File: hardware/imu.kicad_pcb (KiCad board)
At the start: 4 copper layers, 40 x 40 mm, 108 parts, among them J1 USB-MINI-B-SMD, J2 DRILL, J3 DRILL, J4 DRILL, J5 DRILL, J6 STACK-UP-LOW, J7 STACK-DOWN, J8 STACK-UP-LOW, J9 STACK-DOWN, P1 CON-SENSOR, P2 CON-SENSOR, SW1 Reset, SW2 Erase, U1 AT91SAM3SXB, U2 82400152, U3 BNO055, U4 LD1117, X1 16Mhz, X2 32.768kHz

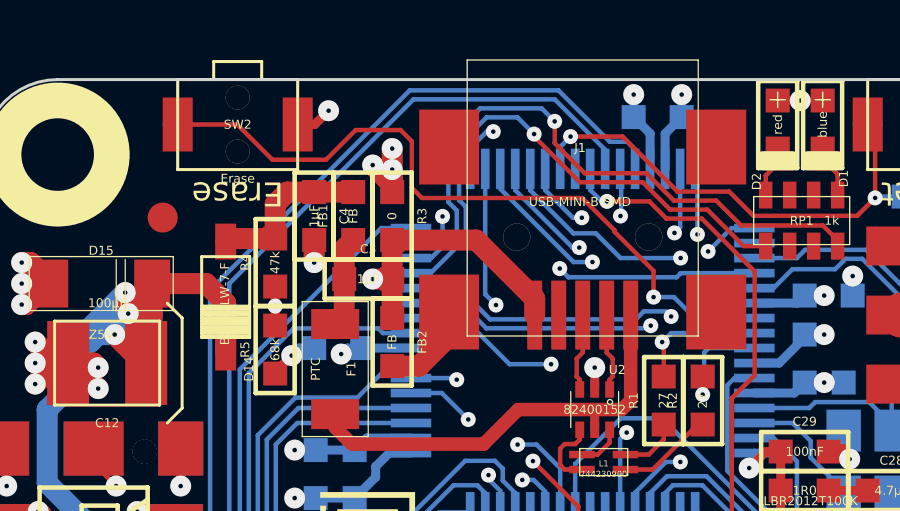
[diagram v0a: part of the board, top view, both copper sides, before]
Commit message: route signals with more distance to border
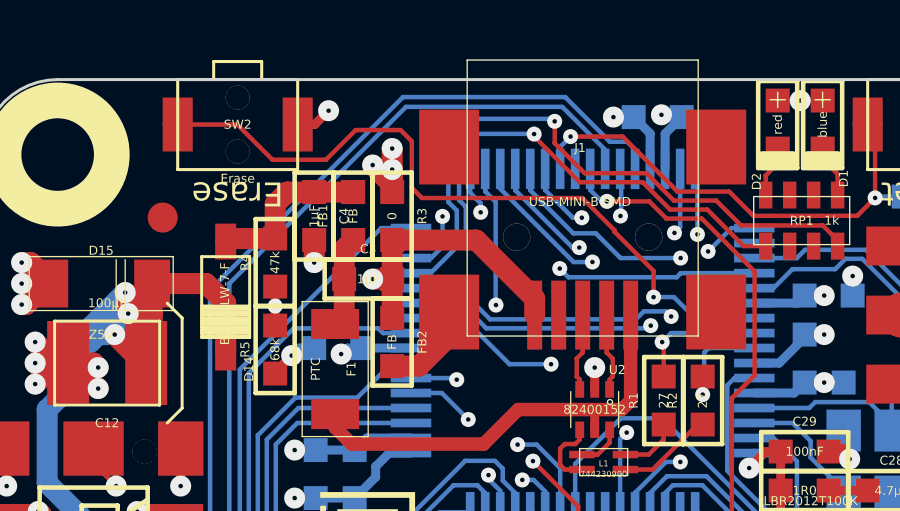
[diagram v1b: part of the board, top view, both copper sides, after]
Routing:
- net STACK-I2C-SDA/JTAG-TDI: track 27.9 -> 27.3 mm

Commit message: change footprint of bno055 crystal
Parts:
- X2: footprint CRYSTAL_3225 -> kicad-libraries:AB26TRQ
- moved C5 3.52 mm to (144.2, 107.5), turned to 180 degrees
- moved C6 2.91 mm to (144.2, 103.9)
- moved X2 1.14 mm to (141.6, 105.7), turned to 270 degrees
- moved R6 0.81 mm to (148.4, 107.5)
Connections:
- C5 pad 1: N-00000128 -> Net-(C5-Pad1)
- C6 pad 1: N-00000133 -> Net-(C6-Pad1)
- U3 pad 26: N-00000133 -> Net-(C6-Pad1)
- U3 pad 27: N-00000128 -> Net-(C5-Pad1)
- X2 pad 1: N-00000128 -> Net-(C6-Pad1)
- X2 pad 2: N-00000133 -> Net-(C5-Pad1)
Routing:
- net N-00000128: track 8.90 -> 0.00 mm, vias 1 -> 0
- net N-00000133: track 6.89 -> 0.00 mm, vias 1 -> 0
- net GND: track 407.8 -> 412.2 mm, vias 78 -> 80
- net Net-(C6-Pad1): track 0.00 -> 4.33 mm, vias 0 -> 1
- net Net-(C5-Pad1): track 0.00 -> 4.08 mm, vias 0 -> 1
- net BNO-BOOT: track 25.6 -> 24.8 mm
- added copper zone on B.Cu, net GND

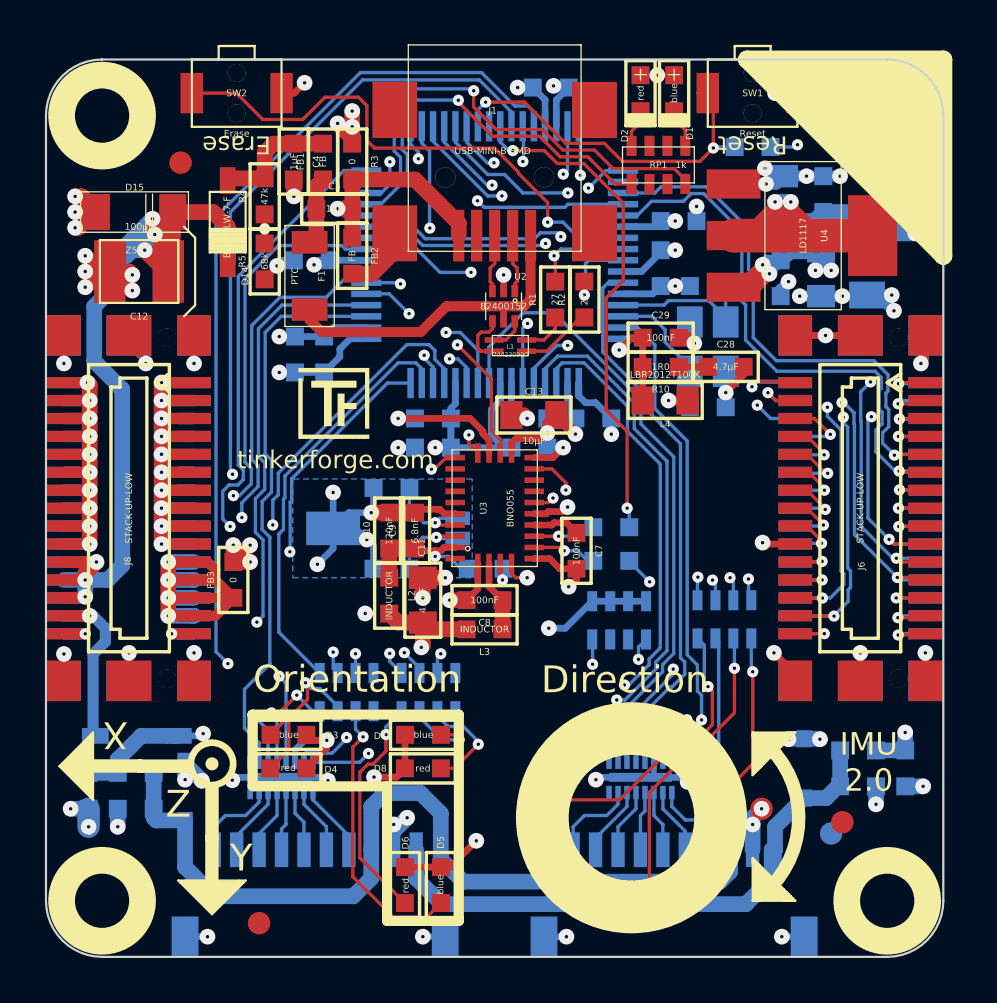
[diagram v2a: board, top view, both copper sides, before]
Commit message: fix tvs diode orientation, fix component texts
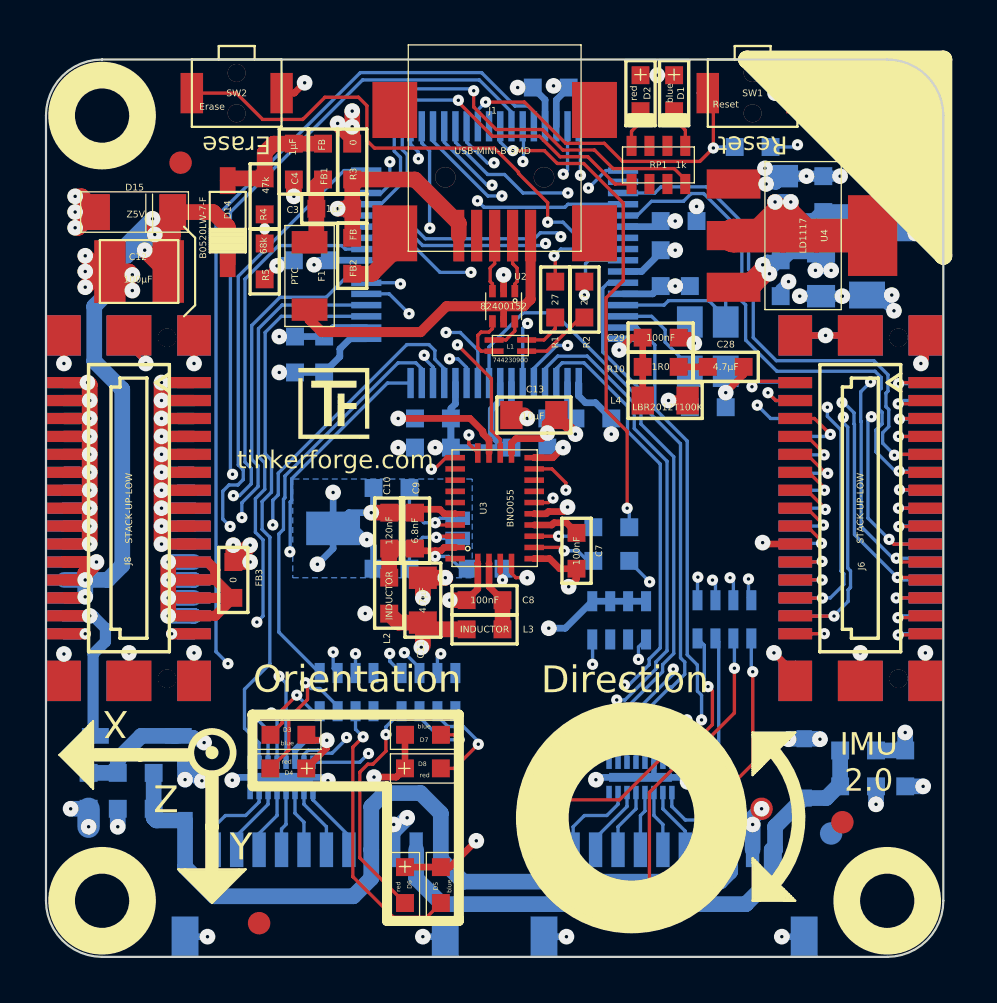
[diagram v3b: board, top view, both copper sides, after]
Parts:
- C1, C2: value 9pF -> DNP
- D10, D11, D12, D4, D6, D8, D9: footprint 0603 -> kicad-libraries:D0603
- D3, D5, D7: footprint 0603 -> kicad-libraries:0603
- turned D401 to 270 degrees
- turned D402 to 270 degrees
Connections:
- D401 pad 1: Net-(C403-Pad1) -> GND
- D401 pad 2: GND -> Net-(C403-Pad1)
- D402 pad 1: Net-(C404-Pad1) -> GND
- D402 pad 2: GND -> Net-(C404-Pad1)

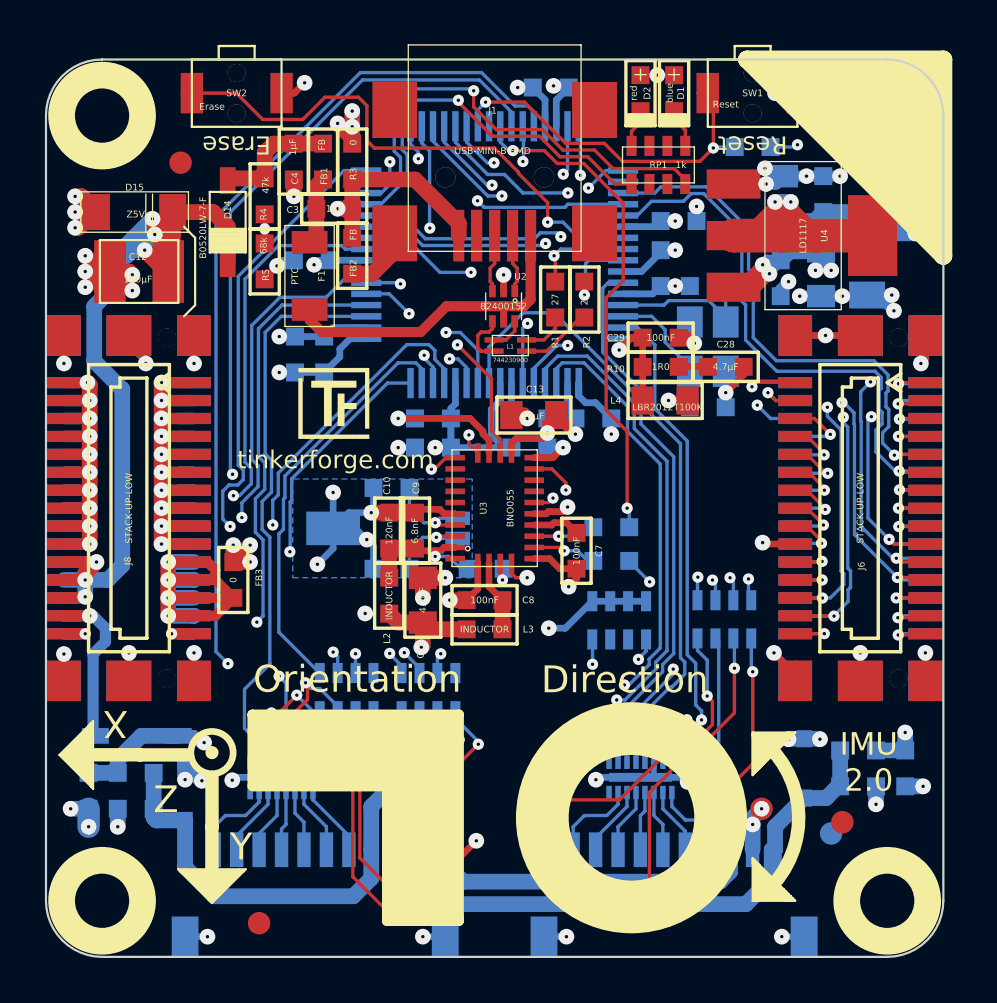
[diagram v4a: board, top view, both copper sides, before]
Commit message: fix diode symbols
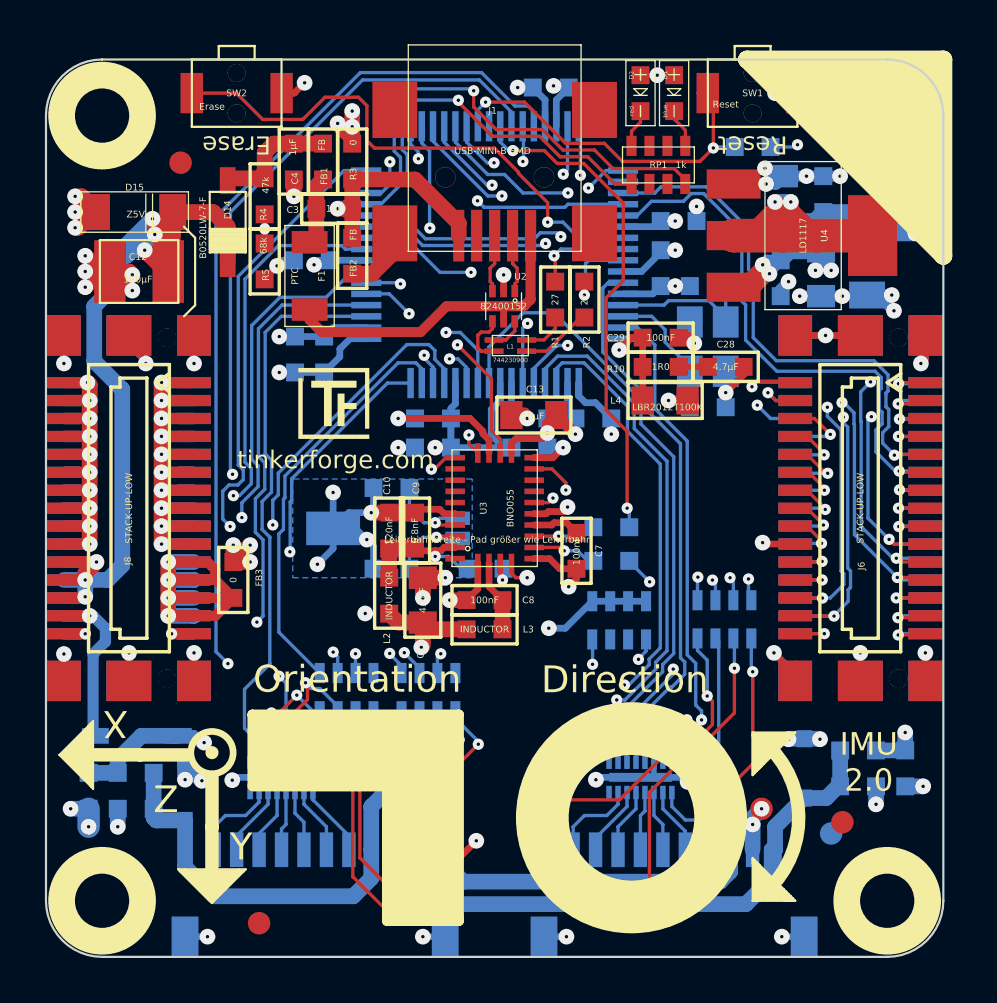
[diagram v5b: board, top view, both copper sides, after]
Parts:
- D1, D2: footprint D0603 -> kicad-libraries:D0603
- D3, D5, D7: footprint kicad-libraries:0603 -> kicad-libraries:D0603
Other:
- board text added: "Leiterbahnbreite - Pad größer wie Leiterbahn"

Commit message: Add some 3d components
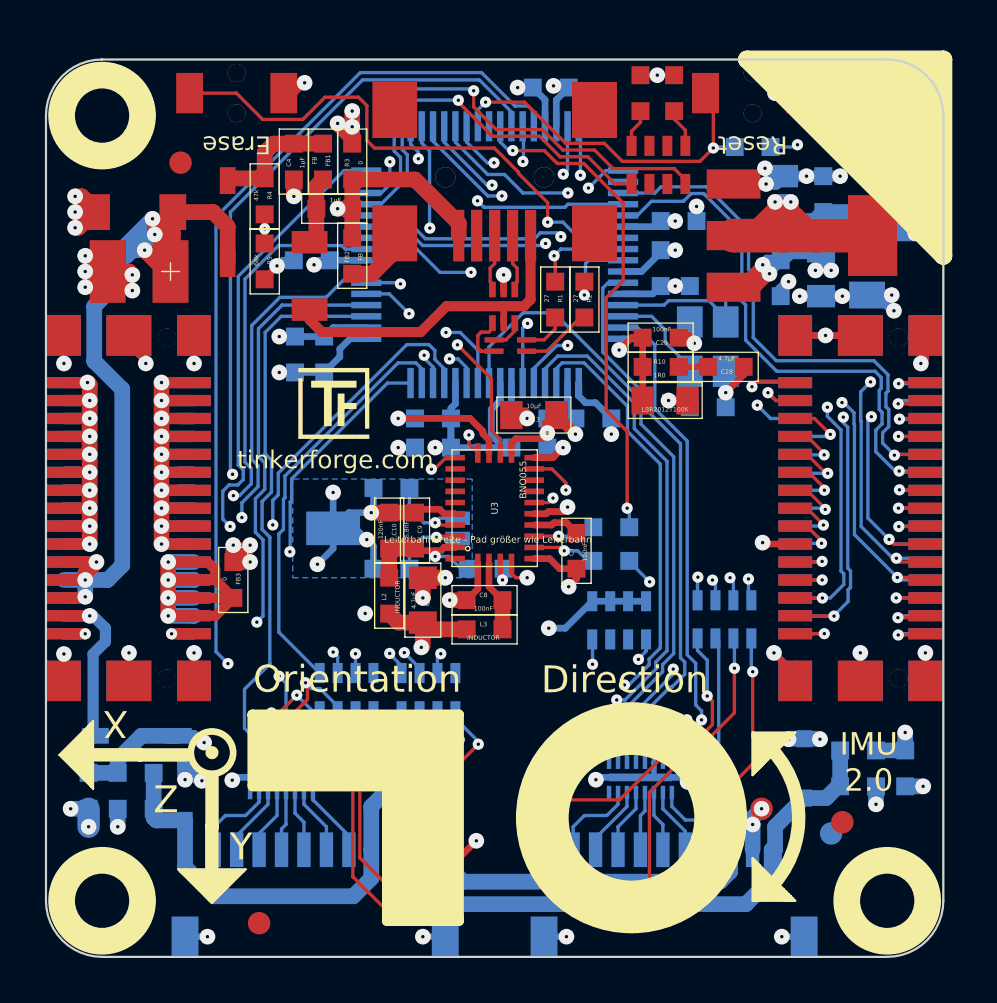
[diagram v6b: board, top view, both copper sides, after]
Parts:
- C1, C10, C14, C15, C17, C18, C19, C2, C20, C21, C22, C23, C24, C26, C27, C28, C29, C3, C30, C4, C401, C402, C403, C404, C5, C6, C7, C8, C9, FB1, FB2, FB3, FB4, FB401, FB402, L2, L3, R1, R10, R2, R3, R4, R5, R6, R7, R8, R9: footprint 0603 -> kicad-libraries:0603
- C11, C13, C16, C25, L4: footprint 0805 -> kicad-libraries:0805
- C12: footprint 3528-21 -> kicad-libraries:3528-21
- D13, D14: footprint SOD-123 -> kicad-libraries:SOD-123
- D15, D16: footprint MiniMelf -> kicad-libraries:MiniMelf
- D401, D402: footprint SOD-323 -> kicad-libraries:SOD-323
- F1: footprint 1206 -> kicad-libraries:1206
- FILTER401, FILTER402: footprint DFN16-33x135 -> kicad-libraries:DFN16-33x135
- J1: footprint USB-MINI-B-SMD -> kicad-libraries:USB-MINI-B-SMD
- J2, J3, J4, J5: footprint DRILL_NP -> kicad-libraries:DRILL_NP
- J6, J8: footprint BTB08-ACS-TOP -> kicad-libraries:BTB08-ACS-TOP
- J7, J9: footprint BTB08-ACS-BTM -> kicad-libraries:BTB08-ACS-BTM
- L1: footprint WE-CNSW-0603 -> kicad-libraries:WE-CNSW-0603
- P1, P2: footprint CON-SENSOR -> kicad-libraries:CON-SENSOR
- RP1, RP2, RP3, RP4, RP5: footprint 0603X4 -> kicad-libraries:0603X4
- SW1, SW2: footprint TACT-SWITCH -> kicad-libraries:TACT-SWITCH
- U1: footprint LQFP64 -> kicad-libraries:LQFP64
- U2: footprint SOT563-SPEC -> kicad-libraries:SOT563-SPEC
- U3: footprint LGA28_5832 -> kicad-libraries:LGA28_5832
- U4: footprint SOT-223 -> kicad-libraries:SOT-223
- X1: footprint CRYSTAL_3225 -> kicad-libraries:CRYSTAL_3225

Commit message: Add all 3d information
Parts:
- C1, C10, C14, C15, C17, C18, C19, C2, C20, C21, C22, C23, C24, C26, C27, C28, C29, C30, C4, C401, C402, C403, C404, C5, C6, C7, C8, C9, FB1, FB2, FB3, FB4, L2, L3: footprint kicad-libraries:0603 -> kicad-libraries:C0603
- C11, C13, C16, C25, L4: footprint kicad-libraries:0805 -> kicad-libraries:C0805
- F1: footprint kicad-libraries:1206 -> kicad-libraries:C1206
- FB401, FB402: footprint kicad-libraries:0603 -> C0603
- FILTER401, FILTER402: footprint kicad-libraries:DFN16-33x135 -> DFN16-33x135
- R1, R10, R2, R3, R4, R5, R6, R7, R8, R9: footprint kicad-libraries:0603 -> kicad-libraries:R0603
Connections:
- FILTER401 pad 8: (no net) -> Net-(FILTER401-Pad8)
- FILTER401 pad 9: (no net) -> Net-(FILTER401-Pad9)
- FILTER402 pad 8: (no net) -> Net-(FILTER402-Pad8)
- FILTER402 pad 9: (no net) -> Net-(FILTER402-Pad9)
- J1 pad 4: (no net) -> Net-(J1-Pad4)
- RP1 pad 2: (no net) -> Net-(RP1-Pad2)
- RP1 pad 3: (no net) -> Net-(RP1-Pad3)
- RP1 pad 6: (no net) -> Net-(RP1-Pad6)
- RP1 pad 7: (no net) -> Net-(RP1-Pad7)
- RP2 pad 4: (no net) -> Net-(RP2-Pad4)
- RP2 pad 5: (no net) -> Net-(RP2-Pad5)
- RP3 pad 4: (no net) -> Net-(RP3-Pad4)
- RP3 pad 5: (no net) -> Net-(RP3-Pad5)
- RP5 pad 6: (no net) -> Net-(RP5-Pad6)
- RP5 pad 7: (no net) -> Net-(RP5-Pad7)
- U1 pad 40: (no net) -> Net-(U1-Pad40)
- U1 pad 50: (no net) -> Net-(U1-Pad50)
- U3 pad 1: (no net) -> Net-(U3-Pad1)
- U3 pad 12: (no net) -> Net-(U3-Pad12)
- U3 pad 13: (no net) -> Net-(U3-Pad13)
- U3 pad 21: (no net) -> Net-(U3-Pad21)
- U3 pad 22: (no net) -> Net-(U3-Pad22)
- U3 pad 23: (no net) -> Net-(U3-Pad23)
- U3 pad 24: (no net) -> Net-(U3-Pad24)
